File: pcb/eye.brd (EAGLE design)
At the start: 101.6 x 101.6 mm, 38 parts, among them J1 3-PIN SMD, J2 3-PIN SMD, U1 WS2812, U10 WS2812, U11 WS2812, U12 WS2812, U13 WS2812, U14 WS2812, U15 WS2812, U16 WS2812, U17 WS2812, U18 WS2812, U19 WS2812, U2 WS2812, U20 WS2812, U21 WS2812, U22 WS2812, U23 WS2812, U24 WS2812, U25 WS2812, U26 WS2812, U27 WS2812, U28 WS2812, U29 WS2812, U3 WS2812, U30 WS2812, U4 WS2812, U5 WS2812, U6 WS2812, U7 WS2812, U8 WS2812, U9 WS2812

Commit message: finish wiring
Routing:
- net N$5: track 0.00 -> 66.3 mm, vias 0 -> 2
- net N$15: track 0.00 -> 66.3 mm, vias 0 -> 2
- net N$10: track 0.00 -> 66.3 mm, vias 0 -> 2
- net N$25: track 0.00 -> 66.3 mm, vias 0 -> 2
- net N$20: track 0.00 -> 66.3 mm, vias 0 -> 2
- net N$31: track 0.00 -> 65.6 mm
- net GND: track 82.7 -> 96.5 mm
- net N$30: track 0.00 -> 6.36 mm
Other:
- board size 101.6 x 101.6 mm -> 70 x 55 mm

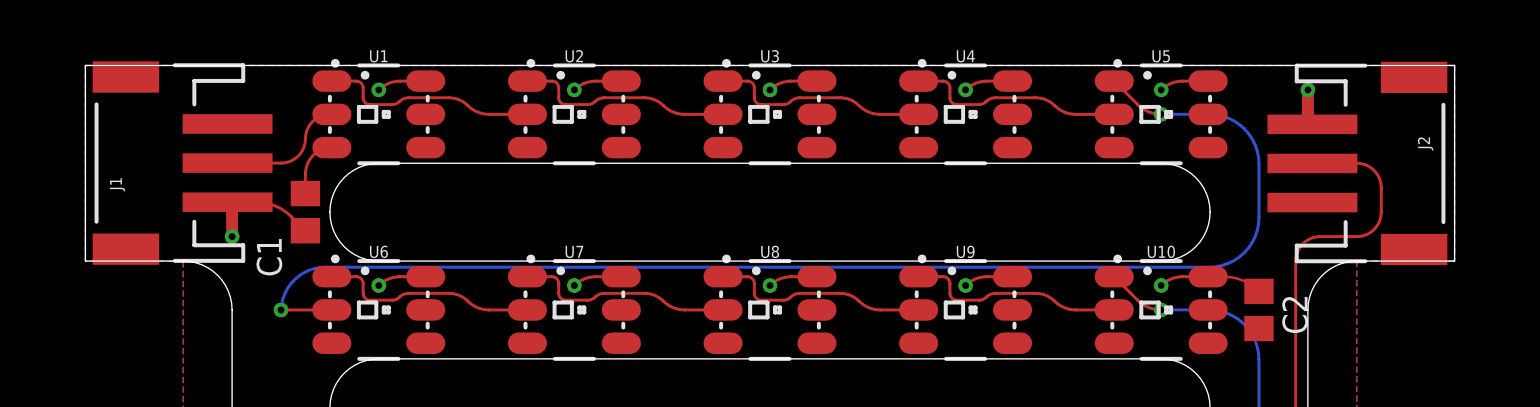
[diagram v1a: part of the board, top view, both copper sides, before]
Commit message: change connector to TE AMP 171826-3
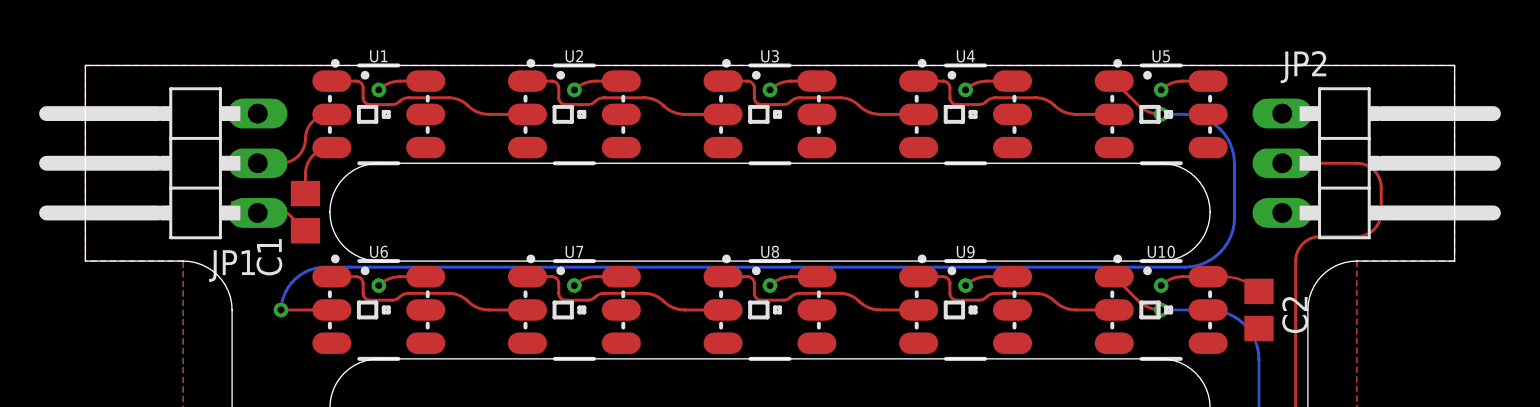
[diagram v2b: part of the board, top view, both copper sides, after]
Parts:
- removed J1, J2: 3-PIN SMD, SparkFun-Connectors:JST-3-SMD
- added JP1, JP2: (no value), pinhead:1X03/90
- added U$1: (no value), josh:SIGNATURE
- added U$2: (no value), josh:LOGO_SILKSCREEN
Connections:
- net +5V: now also JP1.3, JP2.3; no longer J1.3, J2.3
- net GND: now also JP1.1, JP2.1; no longer J1.1, J2.1
- net N$30: now also JP1.2; no longer J1.2
- net N$31: now also JP2.2; no longer J2.2
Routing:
- net GND: track 96.5 -> 92.6 mm, vias 32 -> 30
- net N$30: track 6.36 -> 3.62 mm
- net N$5: track 66.3 -> 63.8 mm
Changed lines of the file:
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@@
 <layer number="115" name="ReferenceISLANDS" color="7" fill="1" visible="no" active="no"/>
 <layer number="116" name="Patch_BOT" color="9" fill="4" visible="no" active="no"/>
+<layer number="117" name="PM_Ref" color="7" fill="1" visible="no" active="no"/>
 <layer number="118" name="Rect_Pads" color="7" fill="1" visible="no" active="no"/>
+<layer number="119" name="PF_Ref" color="7" fill="1" visible="no" active="no"/>
+<layer number="120" name="WFL_Ref" color="7" fill="1" visible="no" active="no"/>
 <layer number="121" name="_tsilk" color="7" fill="1" visible="no" active="no"/>
 <layer number="122" name="_bsilk" color="7" fill="1" visible="no" active="no"/>
@@
 <attribute name="VALUE" x="62.54" y="1.23" size="1.27" layer="27" rot="R90"/>
 </element>
-<element name="J1" library="SparkFun-Connectors" library_urn="urn:adsk.eagle:library:513" package="JST-3-SMD" package3d_urn="urn:adsk.eagle:package:38075/1" value="3-PIN SMD" x="2.5" y="50" smashed="yes" rot="R90">
-<attribute name="NAME" x="1.865" y="48.603" size="0.6096" layer="25" font="vector" ratio="20" rot="R90"/>
-<attribute name="PROD_ID" value="CONN-12591" x="10.12" y="69.05" size="1.778" layer="27" rot="R90" display="off"/>
-<attribute name="VALUE" x="3.77" y="48.349" size="0.6096" layer="27" font="vector" ratio="20" rot="R90"/>
-</element>
-<element name="J2" library="SparkFun-Connectors" library_urn="urn:adsk.eagle:library:513" package="JST-3-SMD" package3d_urn="urn:adsk.eagle:package:38075/1" value="3-PIN SMD" x="67.5" y="50" smashed="yes" rot="R270">
-<attribute name="NAME" x="68.135" y="51.397" size="0.6096" layer="25" font="vector" ratio="20" rot="R270"/>
-<attribute name="PROD_ID" value="CONN-12591" x="59.88" y="19.52" size="1.778" layer="27" rot="R270" display="off"/>
-<attribute name="VALUE" x="66.23" y="51.651" size="0.6096" layer="27" font="vector" ratio="20" rot="R270"/>
-</element>
 <element name="U1" library="SparkFun-LED" package="LED-TRICOLOR-5050-IC" value="WS2812" x="15" y="52.5" smashed="yes">
 <attribute name="NAME" x="15" y="55.167" size="0.6096" layer="25" font="vector" ratio="20" align="bottom-center"/>
@@
 <attribute name="VALUE" x="45" y="39.833" size="0.6096" layer="27" font="vector" ratio="20" align="top-center"/>
 </element>
+<element name="JP1" library="pinhead" library_urn="urn:adsk.eagle:library:325" package="1X03/90" package3d_urn="urn:adsk.eagle:package:22459/2" value="" x="5" y="50" smashed="yes" rot="R90">
+<attribute name="NAME" x="8.81" y="45.555" size="1.27" layer="25" ratio="10" rot="R180"/>
+<attribute name="POPULARITY" value="17" x="5" y="50" size="1.778" layer="27" rot="R90" display="off"/>
+<attribute name="VALUE" x="8.81" y="55.715" size="1.27" layer="27" rot="R180"/>
+</element>
+<element name="JP2" library="pinhead" library_urn="urn:adsk.eagle:library:325" package="1X03/90" package3d_urn="urn:adsk.eagle:package:22459/2" value="" x="65" y="50" smashed="yes" rot="R270">
+<attribute name="NAME" x="61.19" y="54.445" size="1.27" layer="25" ratio="10"/>
+<attribute name="POPULARITY" value="17" x="65" y="50" size="1.778" layer="27" rot="R270" display="off"/>
+<attribute name="VALUE" x="61.19" y="44.285" size="1.27" layer="27"/>
+</element>
+<element name="U$1" library="josh" package="SIGNATURE" value="" x="52.5" y="41.25" smashed="yes" rot="MR0"/>
+<element name="U$2" library="josh" package="LOGO_SILKSCREEN" value="" x="11.25" y="41.5625" smashed="yes" rot="MR0"/>
 </elements>
 <signals>
@@
 <wire x1="53.805025" y1="52.994975" x2="55" y2="52.5" width="0.1524" layer="1" curve="45"/>
 <via x="55" y="52.5" extent="1-16" drill="0.35"/>
-<wire x1="55" y1="52.5" x2="57.46" y2="52.5" width="0.1524" layer="16"/>
-<wire x1="57.46" y1="52.5" x2="60" y2="49.96" width="0.1524" layer="16" curve="-90"/>
-<wire x1="60" y1="47.2275" x2="57.46" y2="44.6875" width="0.1524" layer="16" curve="-90"/>
+<wire x1="55" y1="52.5" x2="56.21" y2="52.5" width="0.1524" layer="16"/>
+<wire x1="56.21" y1="52.5" x2="58.75" y2="49.96" width="0.1524" layer="16" curve="-90"/>
+<wire x1="58.75" y1="47.2275" x2="56.21" y2="44.6875" width="0.1524" layer="16" curve="-90"/>
 <wire x1="12.375" y1="44.6875" x2="10" y2="42.5" width="0.1524" layer="16" curve="90"/>
 <via x="10" y="42.5" extent="1-16" drill="0.35"/>
 <wire x1="10" y1="42.5" x2="12.6" y2="42.5" width="0.1524" layer="1"/>
-<wire x1="60" y1="49.96" x2="60" y2="47.2275" width="0.1524" layer="16"/>
-<wire x1="57.46" y1="44.6875" x2="12.375" y2="44.6875" width="0.1524" layer="16"/>
+<wire x1="58.75" y1="49.96" x2="58.75" y2="47.2275" width="0.1524" layer="16"/>
+<wire x1="56.21" y1="44.6875" x2="12.375" y2="44.6875" width="0.1524" layer="16"/>
 </signal>
 <signal name="+5V">
@@
 <contactref element="C5" pad="1"/>
 <contactref element="C6" pad="1"/>
-<contactref element="J1" pad="3"/>
-<contactref element="J2" pad="3"/>
 <polygon width="0.1524" layer="1">
 <vertex x="0" y="55"/>
@@
 <wire x1="11.25" y1="48.45" x2="11.25" y2="49.45" width="0.1524" layer="1"/>
 <wire x1="11.25" y1="49.45" x2="12.6" y2="50.8" width="0.1524" layer="1" curve="-90"/>
+<contactref element="JP1" pad="3"/>
+<contactref element="JP2" pad="3"/>
 </signal>
 <signal name="GND">
@@
 <contactref element="C5" pad="2"/>
 <contactref element="C6" pad="2"/>
-<contactref element="J1" pad="1"/>
-<contactref element="J2" pad="1"/>
 <polygon width="0.1524" layer="16">
 <vertex x="70" y="55"/>
@@
 <wire x1="8.737896875" y1="48.01" x2="10.53395" y2="47.26605" width="0.1524" layer="1" curve="-45"/>
 <wire x1="10.53395" y1="47.26605" x2="11.25" y2="46.55" width="0.1524" layer="1"/>
-<via x="7.5" y="46.25" extent="1-16" drill="0.35"/>
-<wire x1="7.27" y1="48.01" x2="7.5" y2="48.01" width="0.6096" layer="1"/>
-<wire x1="7.27" y1="48.01" x2="7.302009375" y2="47.977990625" width="0.6096" layer="1"/>
-<wire x1="7.302009375" y1="47.977990625" x2="7.5" y2="47.5" width="0.6096" layer="1" curve="-45"/>
-<wire x1="7.5" y1="47.5" x2="7.5" y2="46.25" width="0.6096" layer="1"/>
-<wire x1="62.73" y1="51.99" x2="62.697990625" y2="52.022009375" width="0.6096" layer="1"/>
-<wire x1="62.697990625" y1="52.022009375" x2="62.5" y2="52.5" width="0.6096" layer="1" curve="-45"/>
-<wire x1="62.5" y1="52.5" x2="62.5" y2="53.75" width="0.6096" layer="1"/>
-<via x="62.5" y="53.75" extent="1-16" drill="0.35"/>
 <wire x1="57.4" y1="14.2" x2="58.197896875" y2="14.2" width="0.127" layer="1"/>
 <wire x1="58.197896875" y1="14.2" x2="59.99395" y2="13.45605" width="0.127" layer="1" curve="-45"/>
@@
 <wire x1="58.197896875" y1="4.2" x2="59.99395" y2="3.45605" width="0.127" layer="1" curve="-45"/>
 <wire x1="59.99395" y1="3.45605" x2="60" y2="3.45" width="0.127" layer="1"/>
+<contactref element="JP1" pad="1"/>
+<contactref element="JP2" pad="1"/>
+<wire x1="8.81" y1="47.46" x2="7.5" y2="48.01" width="0" layer="19" extent="1-1"/>
 </signal>
 <signal name="N$6">
@@
 <signal name="N$31">
 <contactref element="U30" pad="1"/>
-<contactref element="J2" pad="2"/>
-<wire x1="62.72" y1="50" x2="62.73" y2="49.99" width="0.1524" layer="1" curve="-90"/>
 <wire x1="52.6" y1="4.2" x2="53.368196875" y2="3.881803125" width="0.1524" layer="1" curve="-45"/>
 <wire x1="54.85605" y1="2.39395" x2="56.652103125" y2="1.65" width="0.1524" layer="1" curve="45"/>
@@
 <wire x1="65" y1="50" x2="62.72" y2="50" width="0.1524" layer="1"/>
 <wire x1="61.875" y1="1.375" x2="61.875" y2="45" width="0.1524" layer="1"/>
+<contactref element="JP2" pad="2"/>
+<wire x1="62.72" y1="50" x2="61.19" y2="50" width="0" layer="19" extent="1-1"/>
 </signal>
 <signal name="N$30">
-<contactref element="J1" pad="2"/>
 <contactref element="U1" pad="2" route="any" routetag="U1.DI"/>
-<wire x1="7.27" y1="50.01" x2="10.01" y2="50.01" width="0.1524" layer="1"/>
 <wire x1="10.01" y1="50.01" x2="11.25" y2="51.25" width="0.1524" layer="1" curve="90"/>
 <wire x1="11.25" y1="51.25" x2="12.5" y2="52.5" width="0.1524" layer="1" curve="-90"/>
 <wire x1="12.5" y1="52.5" x2="12.6" y2="52.5" width="0.1524" layer="1"/>
+<contactref element="JP1" pad="2"/>
+<wire x1="8.81" y1="50" x2="10.01" y2="50.01" width="0" layer="19" extent="1-1"/>
 </signal>
 </signals>

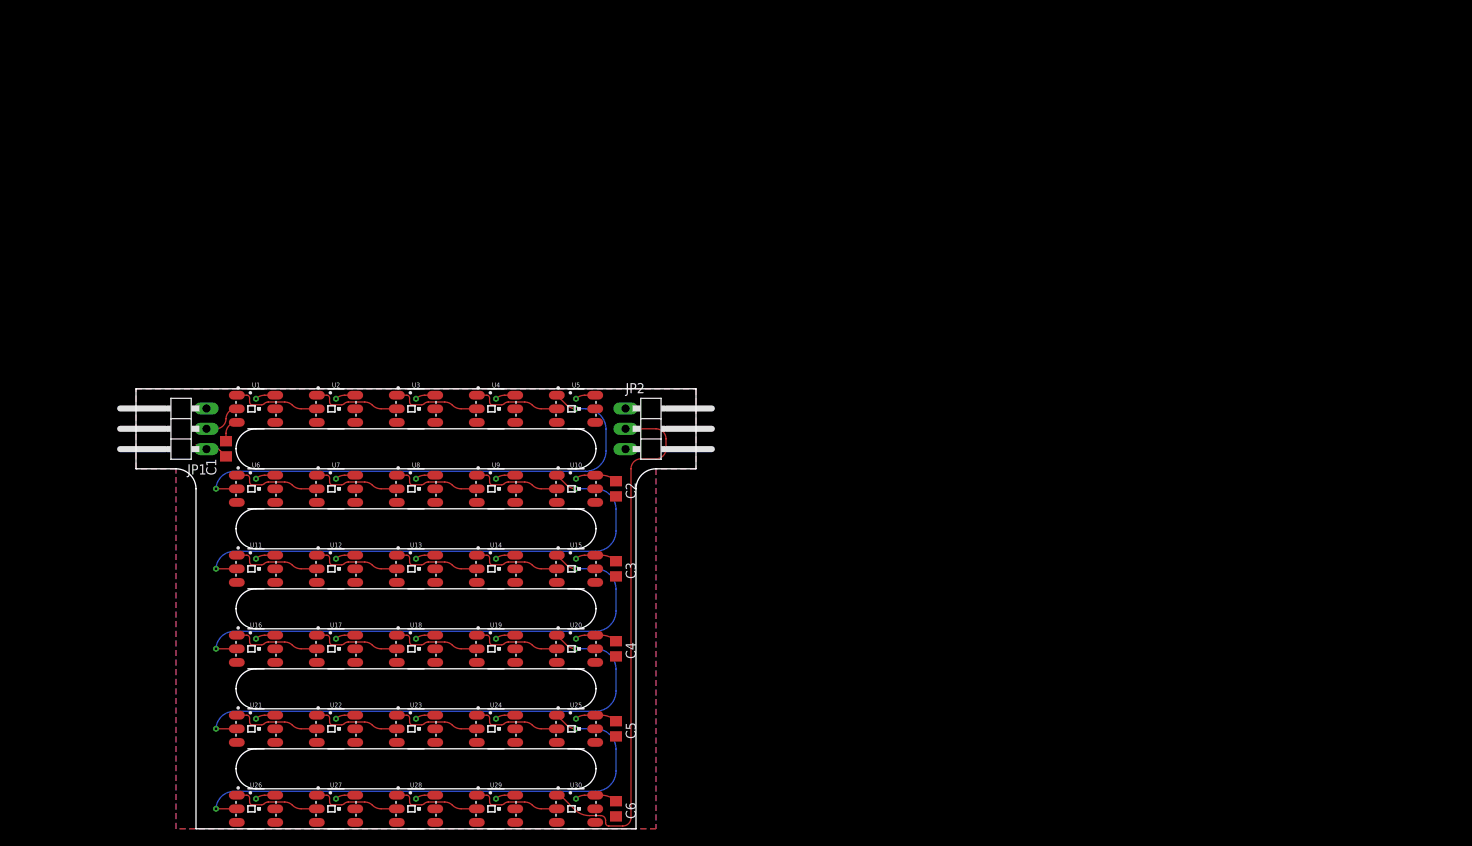
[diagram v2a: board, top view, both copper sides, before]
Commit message: make full glasses and add mcu to them
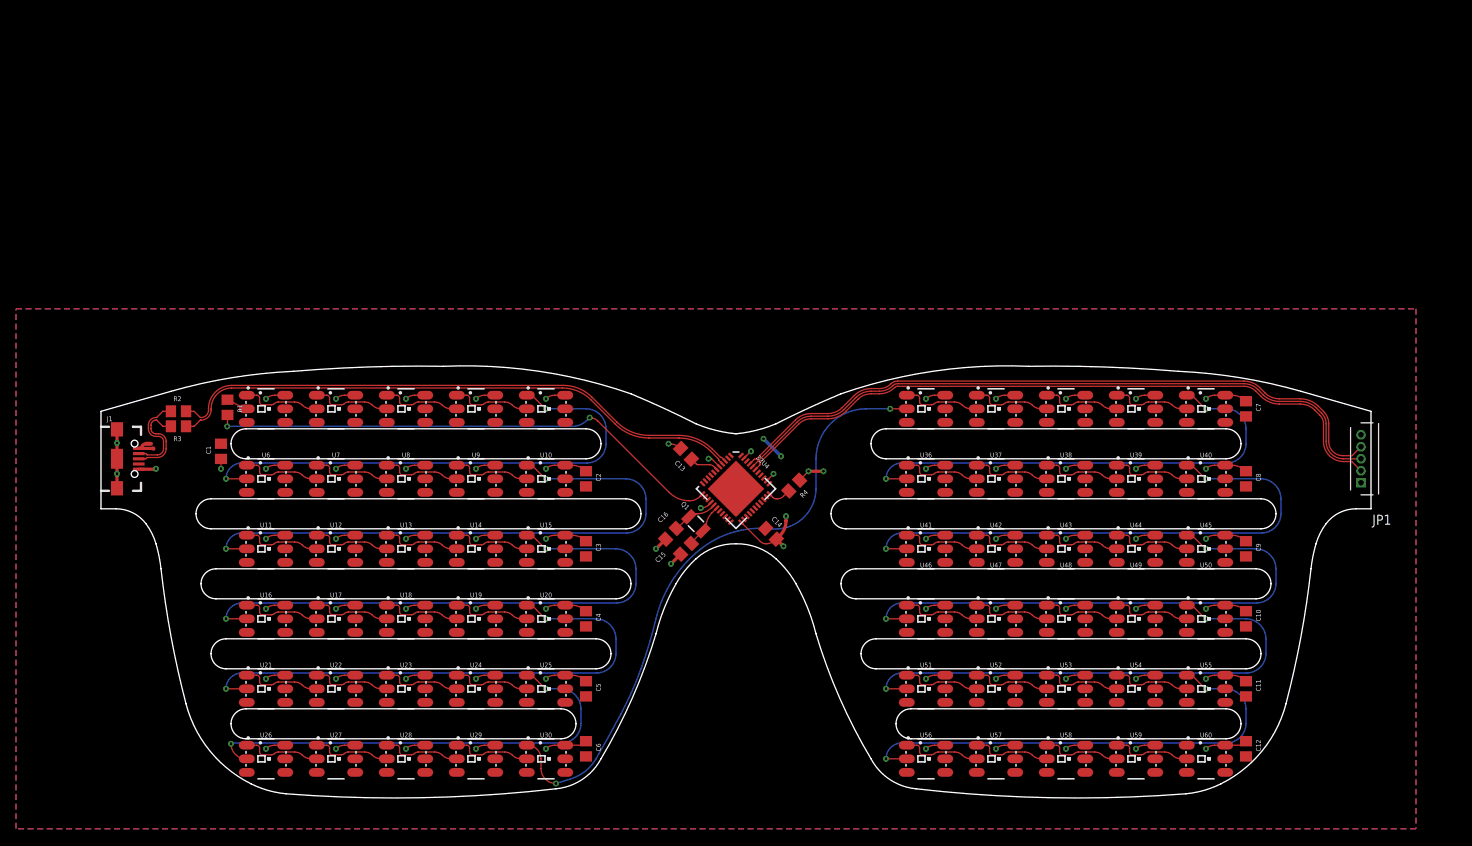
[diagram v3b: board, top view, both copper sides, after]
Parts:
- removed JP2: (no value), pinhead:1X03/90
- added 32U4: 32U4, SparkFun-IC-Microcontroller:QFN-44
- added C10, C11, C12, C7, C8, C9: (no value), rcl:C0805
- added C13, C14: 1u, rcl:C0805
- added C15, C16: 20p, rcl:C0805
- added J1: (no value), SparkFun-Connectors:USB-B-MICRO-SMD
- added Q1: ECS-160-20-3X-TR, SparkFun-Clocks:CRYSTAL-SMD-3.2X1.5MM
- added R1: 470, rcl:R0805
- added R2, R3: 22, rcl:R0805
- added R4: 1k, rcl:R0805
- added U31, U32, U33, U34, U35, U36, U37, U38, U39, U40, U41, U42, U43, U44, U45, U46, U47, U48, U49, U50, U51, U52, U53, U54, U55, U56, U57, U58, U59, U60: WS2812, SparkFun-LED:LED-TRICOLOR-5050-IC
- JP1: value (none) -> JST-ZH-5; device pinhead:1X03/90 -> josh:JST-ZH-5-TH
- moved JP1 148.2 mm to (153.1, 46.2)
- moved U$2 63.8 mm to (75.0, 44.7)
- moved U$1 22.8 mm to (75.0, 37.5)
- moved C6 8.39 mm to (56.2, 10.0)
- moved U30 7.29 mm to (51.2, 8.75)
- moved U29 6.73 mm to (42.5, 8.75)
- moved U26 6.37 mm to (16.2, 8.75)
- moved U28 6.37 mm to (33.8, 8.75)
- moved C5 6.25 mm to (56.2, 17.5)
- moved U25 6.25 mm to (51.2, 17.5)
- moved U27 6.25 mm to (25.0, 8.75)
- moved U24 5.59 mm to (42.5, 17.5)
- moved C4 5.30 mm to (56.2, 26.2)
- moved U20 5.30 mm to (51.2, 26.2)
- moved U21 5.15 mm to (16.2, 17.5)
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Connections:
- new net LED_DATA: 32U4.12, R1.1
- new net N$32: U32.1, U33.2
- new net N$33: U33.1, U34.2
- new net N$34: U34.1, U35.2
- new net N$35: U35.1, U36.2
- new net N$36: U36.1, U37.2
- new net N$37: U37.1, U38.2
- new net N$38: U38.1, U39.2
- new net N$39: U39.1, U40.2
- new net N$40: U40.1, U41.2
- new net N$41: U41.1, U42.2
- new net N$42: U42.1, U43.2
- new net N$43: U43.1, U44.2
- new net N$44: U44.1, U45.2
- new net N$45: U45.1, U46.2
- new net N$46: U46.1, U47.2
- new net N$47: U47.1, U48.2
- new net N$48: U48.1, U49.2
- new net N$49: U49.1, U50.2
- new net N$50: U50.1, U51.2
- new net N$51: U51.1, U52.2
- new net N$52: U52.1, U53.2
- new net N$53: U53.1, U54.2
- new net N$54: U54.1, U55.2
- new net N$55: U55.1, U56.2
- new net N$56: U56.1, U57.2
- new net N$57: U57.1, U58.2
- new net N$58: U58.1, U59.2
- new net N$59: U59.1, U60.2
- new net N$60: U30.1, U31.2
- new net N$61: R1.2, U1.2
- new net N$62: 32U4.6, C13.1
- new net N$63: 32U4.40, JP1.P$3
- new net N$64: 32U4.39, JP1.P$2
- new net N$67: 32U4.16, C16.1, Q1.P$2
- new net N$68: 32U4.17, C15.1, Q1.P$1
- new net N$77: 32U4.33, R4.2
- new net RST: 32U4.13
- new net USB1_N: J1.D-, R2.1
- new net USB1_P: J1.D+, R3.1
- new net USB_N: 32U4.3, R2.2
- new net USB_P: 32U4.4, R3.2
- net +5V: now also 32U4.14, 32U4.2, 32U4.24, 32U4.34, 32U4.42, 32U4.44, 32U4.7, C10.1, C11.1, C12.1, C14.1, C7.1, C8.1, C9.1, J1.VBUS, JP1.P$1, U31.3, U31.5, U32.3, U32.5, U33.3, U33.5, U34.3, U34.5, U35.3, U35.5, U36.3, U36.5, U37.3, U37.5, U38.3, U38.5, U39.3, U39.5, U40.3, U40.5, U41.3, U41.5, U42.3, U42.5, U43.3, U43.5, U44.3, U44.5, U45.3, U45.5, U46.3, U46.5, U47.3, U47.5, U48.3, U48.5, U49.3, U49.5, U50.3, U50.5, U51.3, U51.5, U52.3, U52.5, U53.3, U53.5, U54.3, U54.5, U55.3, U55.5, U56.3, U56.5, U57.3, U57.5, U58.3, U58.5, U59.3, U59.5, U60.3, U60.5; no longer JP1.3, JP2.3
- net GND: now also 32U4.15, 32U4.23, 32U4.35, 32U4.43, 32U4.5, C10.2, C11.2, C12.2, C13.2, C14.2, C15.2, C16.2, C7.2, C8.2, C9.2, J1.GND, J1.SHIELD1, J1.SHIELD2, J1.SHIELD3, JP1.P$5, R4.1, U31.6, U32.6, U33.6, U34.6, U35.6, U36.6, U37.6, U38.6, U39.6, U40.6, U41.6, U42.6, U43.6, U44.6, U45.6, U46.6, U47.6, U48.6, U49.6, U50.6, U51.6, U52.6, U53.6, U54.6, U55.6, U56.6, U57.6, U58.6, U59.6, U60.6; no longer JP1.1, JP2.1
- net N$30: now also 32U4.41, JP1.P$4; no longer JP1.2, U1.2
- net N$31: now also U31.1, U32.2; no longer JP2.2, U30.1
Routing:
- net GND: track 92.6 -> 214.8 mm, vias 30 -> 75
- net N$64: track 0.00 -> 84.9 mm
- net N$63: track 0.00 -> 84.7 mm
- net N$30: track 3.62 -> 85.5 mm
- net N$60: track 0.00 -> 76.1 mm, vias 0 -> 2
- net USB_N: track 0.00 -> 72.4 mm
- net USB_P: track 0.00 -> 72.1 mm
- net N$40: track 0.00 -> 69.1 mm, vias 0 -> 2
- net N$45: track 0.00 -> 67.9 mm, vias 0 -> 2
- net LED_DATA: track 0.00 -> 65.4 mm, vias 0 -> 2
- net N$50: track 0.00 -> 65.4 mm, vias 0 -> 2
- net N$35: track 0.00 -> 60.4 mm, vias 0 -> 2
- net N$55: track 0.00 -> 60.4 mm, vias 0 -> 2
- net N$31: track 65.6 -> 9.78 mm
- net USB1_P: track 0.00 -> 10.9 mm
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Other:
- board size 70 x 55 mm -> 158.8 x 54 mm

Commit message: finish up glasses
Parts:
- added C17, C18, C19: (no value), rcl:C0603
- added U$4, U$5: GLASSES_HINGE, josh:GLASSES_HINGE
- C1, C10, C11, C12, C13, C14, C15, C16, C2, C3, C4, C5, C6, C7, C8, C9: device rcl:C0805 -> rcl:C0603
- JP1: value JST-ZH-5 -> JST-ZH-5SMD-RA; device josh:JST-ZH-5-TH -> josh:JST-ZH-5-SMD-RA
- R1, R2, R3, R4: device rcl:R0805 -> rcl:R0603
- moved 32U4 5.00 mm to (80.0, 42.5)
- moved C1 5.00 mm to (15.6, 47.2)
- moved C10 5.00 mm to (143.8, 26.2)
- moved C11 5.00 mm to (143.8, 17.5)
- moved C12 5.00 mm to (143.8, 10.0)
- moved C13 5.00 mm to (73.8, 46.9)
- moved C14 5.00 mm to (84.4, 36.9)
- moved C15 5.00 mm to (73.8, 35.0)
- moved C16 5.00 mm to (71.9, 36.9)
- moved C2 5.00 mm to (61.2, 43.8)
- moved C3 5.00 mm to (61.2, 35.0)
- moved C4 5.00 mm to (61.2, 26.2)
- moved C5 5.00 mm to (61.2, 17.5)
- moved C6 5.00 mm to (61.2, 10.0)
- moved C7 5.00 mm to (143.8, 52.5)
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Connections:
- net +5V: now also C17.1, C18.1, C19.1
- net GND: now also C17.2, C18.2, C19.2, U$4.P$1, U$4.P$2, U$5.P$1, U$5.P$2
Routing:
- net GND: track 214.8 -> 228.6 mm, vias 75 -> 78
- net N$64: track 84.9 -> 81.1 mm
- net N$63: track 84.7 -> 80.9 mm
- net N$30: track 85.5 -> 81.7 mm
